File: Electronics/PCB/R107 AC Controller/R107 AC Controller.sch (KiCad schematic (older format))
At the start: 56 parts, among them J1 CAR POWER, J2 CONTROL, J3 ACCESSORY, J4 KNOB, J5 THERMOCOUPLE, J6 USB_B_Mini, J7 ISP, K1 G5LE-1, K2 G5LE-1, Q1 MMBT2222ALT1G, Q2 MMBT2222ALT1G, U1 ATmega328P, U2 LM2596S-5, U3 MAX31855KASA, U4 FT232RL, Y1 ECS-160-18-5PX-TR 16MHz

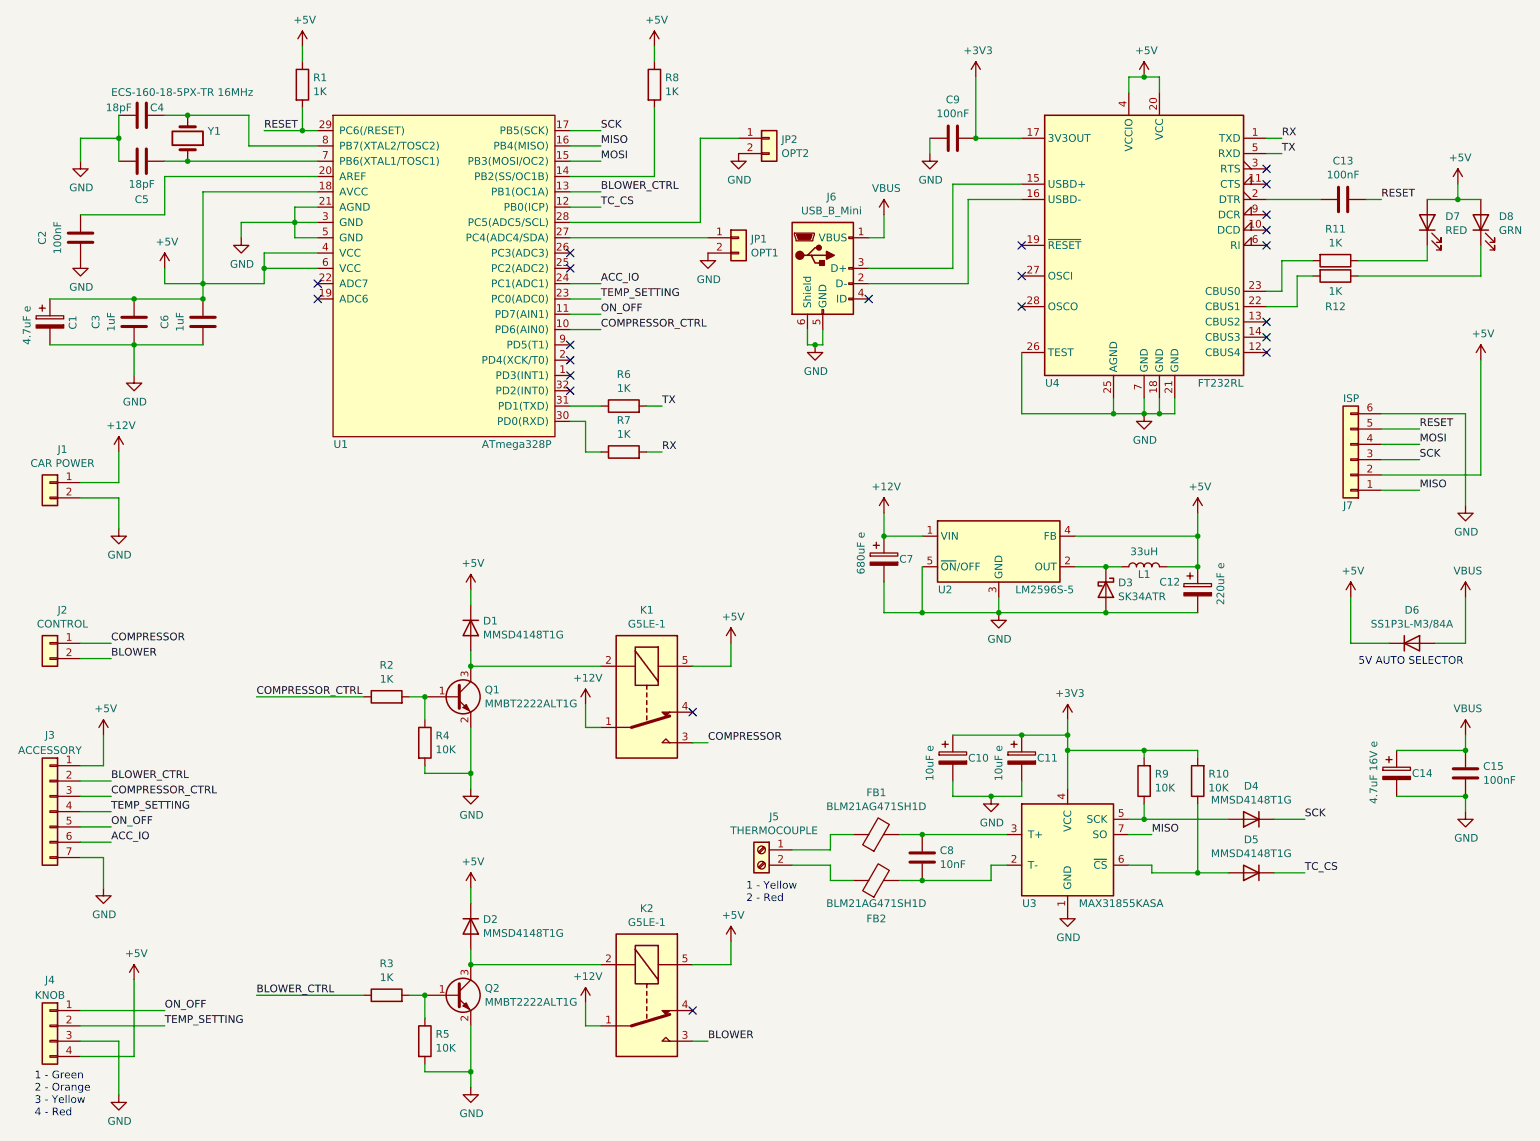
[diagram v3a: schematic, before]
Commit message: Working on PCB. Added status LED and removed comms LEDs. Added jumper to reduce chances of noise on RX input keeping bootloader running.
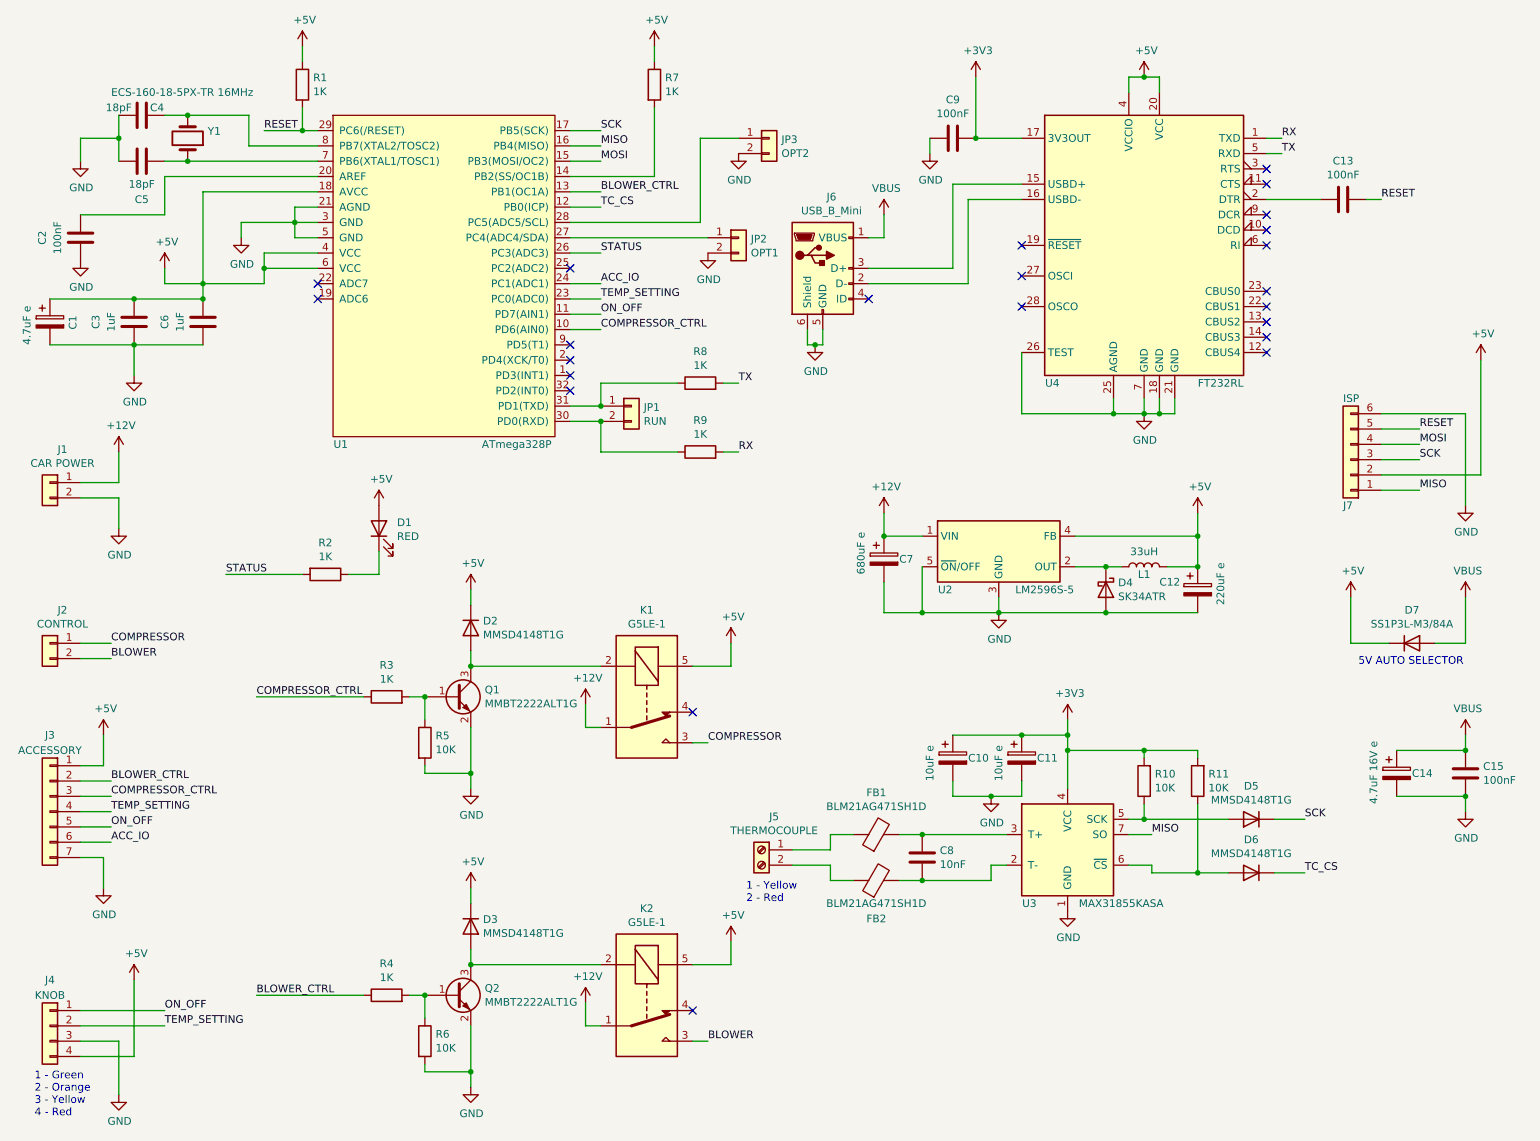
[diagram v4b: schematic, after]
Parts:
- removed D7: RED, LED_SMD:LED_PLCC-2, symbol Device:LED
- removed D8: GRN, LED_SMD:LED_PLCC-2, symbol Device:LED
- removed R11, R12: 1K, Resistor_SMD:R_0805_2012Metric, symbol Device:R
- added D1: RED, LED_SMD:LED_PLCC-2, symbol Device:LED
- added JP1: RUN, Connector_PinHeader_2.54mm:PinHeader_1x02_P2.54mm_Vertical, symbol Connector_Generic:Conn_01x02
- added R2: 1K, Resistor_SMD:R_0805_2012Metric, symbol Device:R
- renumbered D1 to D2, D2 to D3, D3 to D4, D4 to D5, D5 to D6, D6 to D7, JP1 to JP2, JP2 to JP3, R9 to R10, R10 to R11, R2 to R3, R3 to R4, R4 to R5, R5 to R6, R8 to R7, R6 to R8, R7 to R9
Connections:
- net +5V: now also D1.2 (A)
- net STATUS: now reaches U1.26 (PC3(ADC3))
- net STATUS: now also R2.2
- net at R9.1, U1.30 (PD0(RXD)): now also JP1.2 (Pin_2)
- net at R8.1, U1.31 (PD1(TXD)): now also JP1.1 (Pin_1)
- new net: D1.1 (K), R2.1
- no-connect marks 22 -> 23
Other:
- moved on the sheet: R8, R9

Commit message: First attempt at PCB.
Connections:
- net BLOWER_CTRL: now also J3.4 (Pin_4); no longer J3.2 (Pin_2)
- net COMPRESSOR_CTRL: now also J3.2 (Pin_2); no longer J3.3 (Pin_3)
- net ON_OFF: now also J3.3 (Pin_3); no longer J3.5 (Pin_5)
- net TEMP_SETTING: now also J3.5 (Pin_5); no longer J3.4 (Pin_4)
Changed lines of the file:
@@
 Wire Wire Line
 	1000 5750 1200 5750
+Text Label 1200 5850 0    50   ~ 0
+BLOWER_CTRL
 Text Label 1200 5650 0    50   ~ 0
-BLOWER_CTRL
-Text Label 1200 5750 0    50   ~ 0
 COMPRESSOR_CTRL
 $Comp
@@
 Wire Wire Line
 	1000 5950 1200 5950
-Text Label 1200 5850 0    50   ~ 0
+Text Label 1200 5950 0    50   ~ 0
 TEMP_SETTING
-Text Label 1200 5950 0    50   ~ 0
+Text Label 1200 5750 0    50   ~ 0
 ON_OFF
 $Comp

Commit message: Completed 3D models. Fixed mistake with footprint for L1 - was too small.
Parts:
- L1: footprint Britishideas:Chilisin_Power_Inductor_AWVS -> Britishideas:Chilisin_Power_Inductor_AWVS_808040
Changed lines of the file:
@@
 F 0 "L1" V 7900 4250 50  0000 C CNN
 F 1 "33uH" V 8049 4250 50  0000 C CNN
-F 2 "Britishideas:Chilisin_Power_Inductor_AWVS" H 7950 4250 50  0001 C CNN
+F 2 "Britishideas:Chilisin_Power_Inductor_AWVS_808040" H 7950 4250 50  0001 C CNN
 F 3 "~" H 7950 4250 50  0001 C CNN
 	1    7950 4250

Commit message: Changed thermocouple connector to quick disconnect type.
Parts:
- J5: footprint TerminalBlock_TE-Connectivity:TerminalBlock_TE_282834-2_1x02_P2.54mm_Horizontal -> Britishideas:Keystone_SturdiMount_TabConnector_1x2
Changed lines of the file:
@@
 F 0 "J5" H 5368 6317 50  0000 C CNN
 F 1 "THERMOCOUPLE" H 5368 6226 50  0000 C CNN
-F 2 "TerminalBlock_TE-Connectivity:TerminalBlock_TE_282834-2_1x02_P2.54mm_Horizontal" H 5450 6100 50  0001 C CNN
+F 2 "Britishideas:Keystone_SturdiMount_TabConnector_1x2" H 5450 6100 50  0001 C CNN
 F 3 "~" H 5450 6100 50  0001 C CNN
 	1    5450 6100

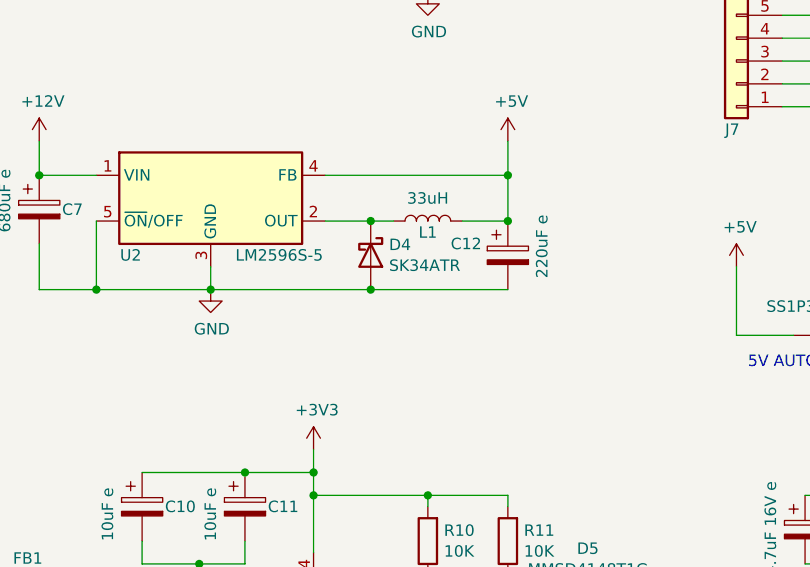
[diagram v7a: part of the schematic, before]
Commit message: Minor silkscreen tweak. Updated part name for diode.
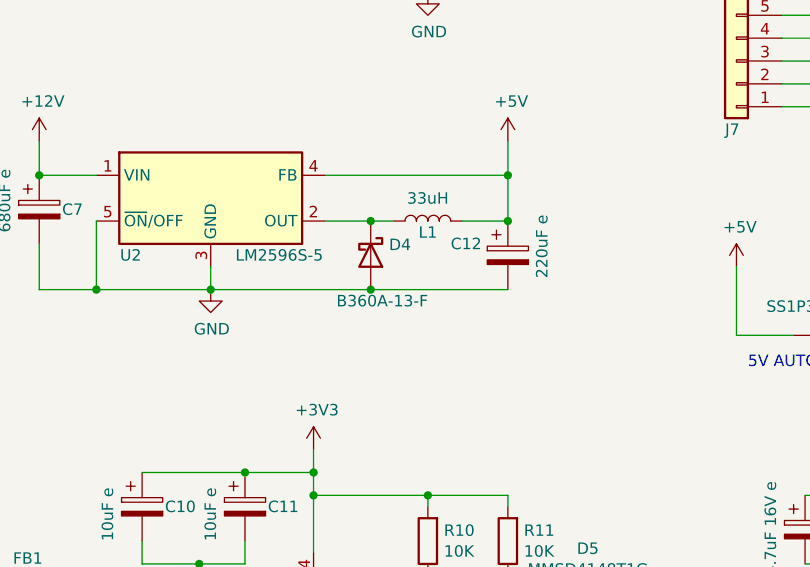
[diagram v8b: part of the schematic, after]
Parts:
- D4: value SK34ATR -> B360A-13-F
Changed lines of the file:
@@
 P 7700 4400
 F 0 "D4" V 7654 4480 50  0000 L CNN
-F 1 "SK34ATR" V 7745 4480 50  0000 L CNN
+F 1 "B360A-13-F" V 7900 4250 50  0000 L CNN
 F 2 "Diode_SMD:D_SMA" H 7700 4400 50  0001 C CNN
 F 3 "~" H 7700 4400 50  0001 C CNN
